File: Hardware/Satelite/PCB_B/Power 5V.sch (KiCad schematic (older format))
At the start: 17 parts, among them IC2 MCP1642B-50I_MS, U5 INA194, U6 MCP6001-OT

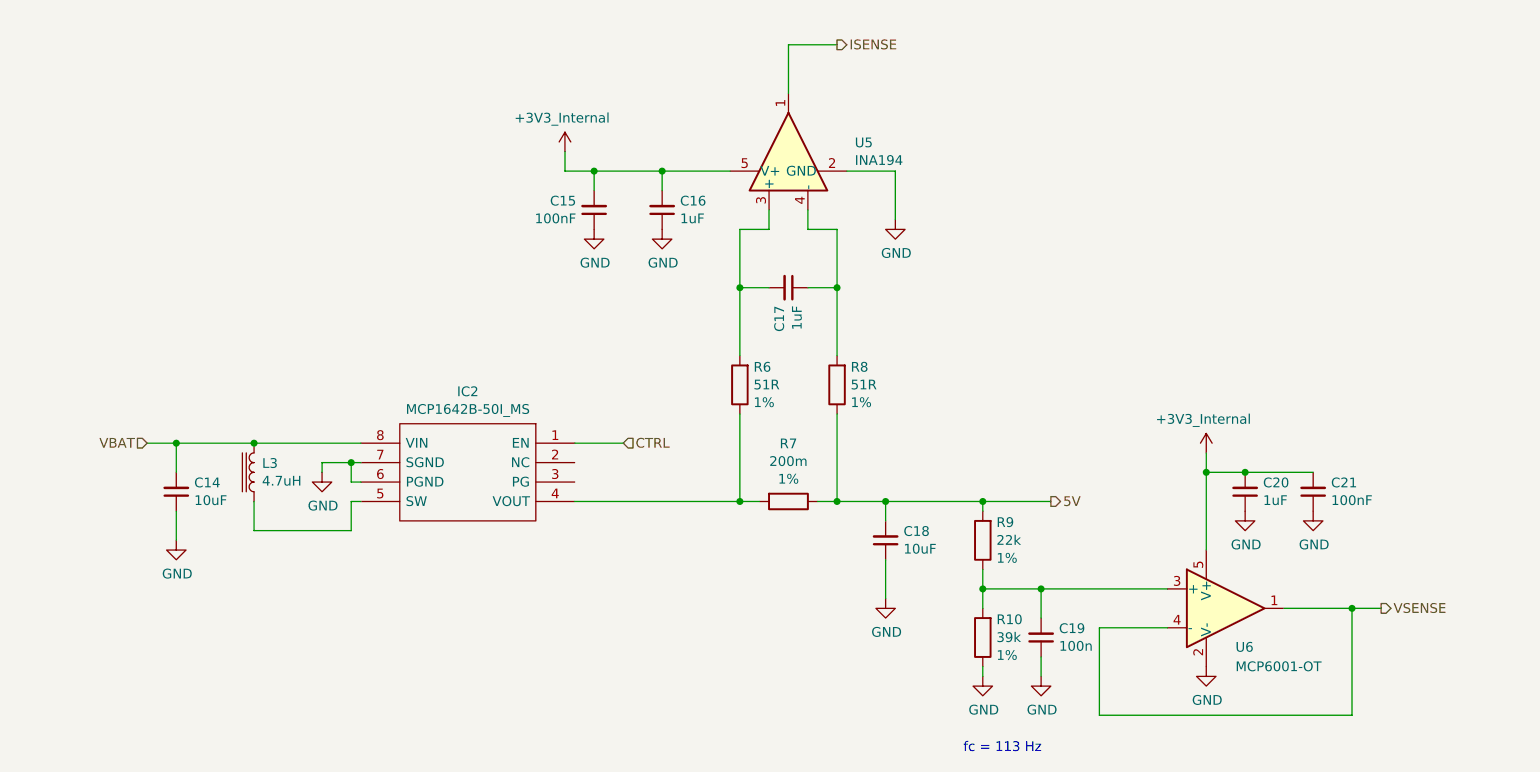
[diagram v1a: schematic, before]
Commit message: Agregado de MOSFET para cortar las fuentes de 3.3V y 5V en el PCB_B en lugar de usar los enable
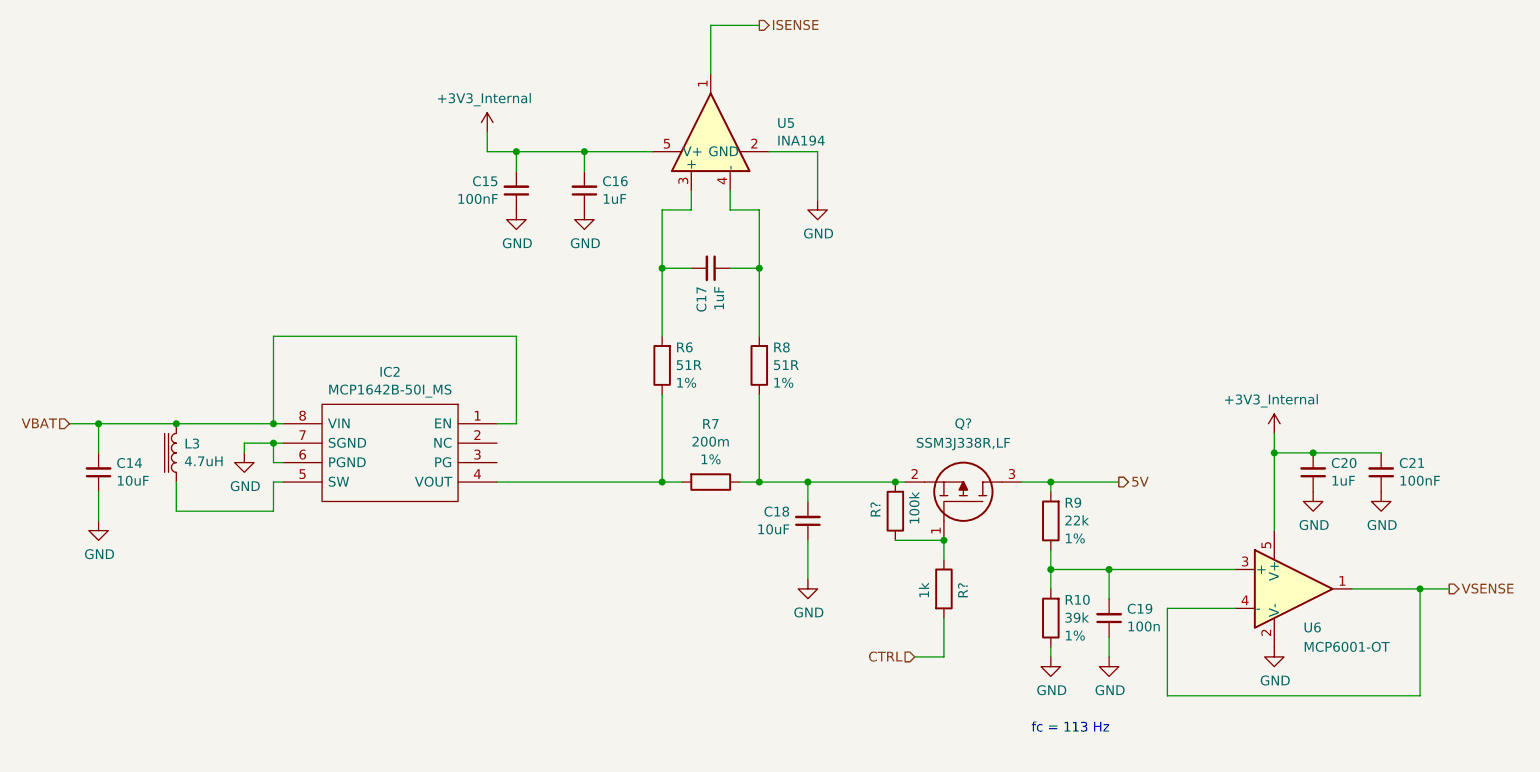
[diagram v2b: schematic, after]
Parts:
- added Q?: SSM3J338R,LF, SamacSys_Parts:SSM3J332RLFT, symbol SamacSys_Parts:SSM3J338R,LF
- added R?: 100k, Resistor_SMD:R_0603_1608Metric_Pad1.05x0.95mm_HandSolder, symbol Device:R
- added R?: 1k, Capacitor_SMD:C_0603_1608Metric_Pad1.05x0.95mm_HandSolder, symbol Device:R
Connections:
- net 5V: now also Q?.3; no longer C18.2, R7.1, R8.1
- net CTRL: now also R?.2; no longer IC2.1 (EN)
- net VBAT: now also IC2.1 (EN)
- new net: C18.2, Q?.2, R7.1, R8.1, R?.2
- new net: Q?.1, R?.1, R?.1
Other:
- moved on the sheet: C14, C15, C16, C17, C18, C19, C20, C21, IC2, L3, R10, R6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

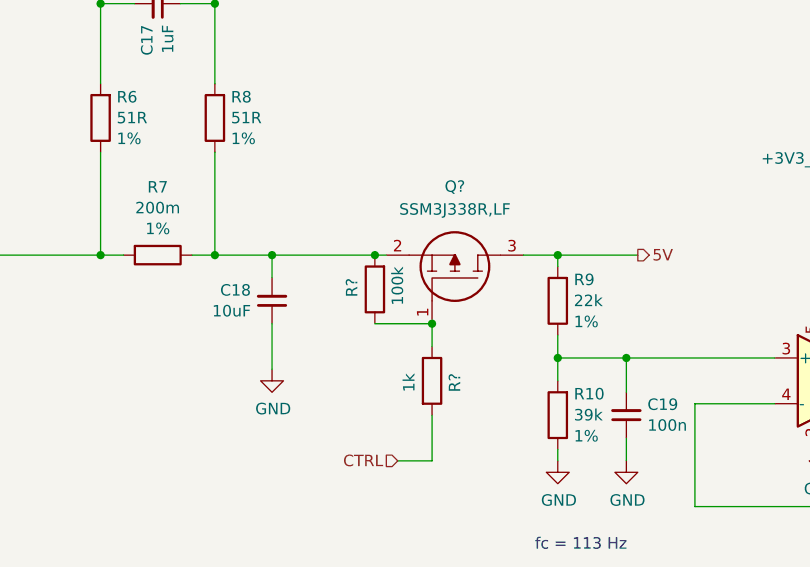
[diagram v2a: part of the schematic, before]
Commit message: Nuevo LDO de más corriente para 3.3V internos en PCB_B
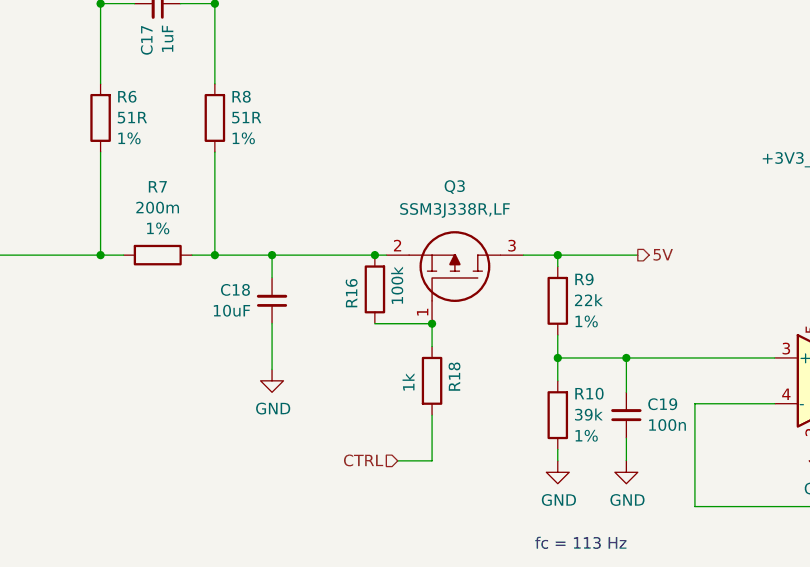
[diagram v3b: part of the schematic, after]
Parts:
- gave numbers to parts that had none: 3
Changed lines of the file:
@@
 P 7050 4600
 AR Path="/5D1EA1A4" Ref="Q?"  Part="1"
-AR Path="/5BC14C3C/5D1EA1A4" Ref="Q?"  Part="1"
-F 0 "Q?" V 7650 4700 50  0000 C CNN
+AR Path="/5BC14C3C/5D1EA1A4" Ref="Q3"  Part="1"
+F 0 "Q3" V 7650 4700 50  0000 C CNN
 F 1 "SSM3J338R,LF" V 7550 4700 50  0000 C CNN
 F 2 "SamacSys_Parts:SSM3J332RLFT" H 7500 4550 50  0001 L CNN
@@
 AR Path="/5BA1A77A/5D221654" Ref="R?"  Part="1"
 AR Path="/5BC300BF/5D221654" Ref="R?"  Part="1"
-AR Path="/5BC14C3C/5D221654" Ref="R?"  Part="1"
-F 0 "R?" V 6900 4400 50  0000 L CNN
+AR Path="/5BC14C3C/5D221654" Ref="R16"  Part="1"
+F 0 "R16" V 6900 4400 50  0000 L CNN
 F 1 "100k" V 6700 4350 50  0000 L CNN
 F 2 "Resistor_SMD:R_0603_1608Metric_Pad1.05x0.95mm_HandSolder" V 6730 4450 50  0001 C CNN
@@
 AR Path="/5BB1631B/5D2253E5" Ref="R?"  Part="1"
 AR Path="/5BC28DAC/5D2253E5" Ref="R?"  Part="1"
-AR Path="/5BC14C3C/5D2253E5" Ref="R?"  Part="1"
-F 0 "R?" V 7150 4800 50  0000 L CNN
+AR Path="/5BC14C3C/5D2253E5" Ref="R18"  Part="1"
+F 0 "R18" V 7150 4800 50  0000 L CNN
 F 1 "1k" V 6950 4800 50  0000 L CNN
 F 2 "Capacitor_SMD:C_0603_1608Metric_Pad1.05x0.95mm_HandSolder" V 6980 4850 50  0001 C CNN

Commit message: PCB_B V2 terminado
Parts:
- IC2: footprint SOP65P490X110-8N -> SamacSys_Parts:SOP65P490X110-8N
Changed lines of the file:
@@
 F 0 "IC2" H 5300 4265 50  0000 C CNN
 F 1 "MCP1642B-50I_MS" H 5300 4174 50  0000 C CNN
-F 2 "SOP65P490X110-8N" H 5700 4100 50  0001 L CNN
+F 2 "SamacSys_Parts:SOP65P490X110-8N" H 5700 4100 50  0001 L CNN
 F 3 "http://ww1.microchip.com/downloads/en/DeviceDoc/20005253A.pdf" H 5700 4000 50  0001 L CNN
 F 4 "Switching Voltage Regulators Step-up DC/DC Reg 1 MHz, 1.6A, 5Vout" H 5700 3900 50  0001 L CNN "Description"
